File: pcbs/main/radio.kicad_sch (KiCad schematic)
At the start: 3 parts

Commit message: Re-routing
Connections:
- net +3V3 renamed +3.3V
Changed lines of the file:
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@@
 			)
 		)
-		(property "Value" "+3V3"
+		(property "Value" "+3.3V"
 			(at 35.5599 60.96 0)
 			(effects

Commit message: Fix pcb
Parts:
- C13: footprint PCM_Capacitor_THT_AKL:C_Disc_D5.0mm_W2.5mm_P2.50mm -> Capacitor_THT:C_Disc_D5.0mm_W2.5mm_P2.50mm
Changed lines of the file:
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@@
 		)
 		(instances
-			(project ""
+			(project "main"
 				(path "/8ab8953a-1156-4e8b-85bc-154005b38a27/95ef0ac5-d3bd-43eb-894b-cca92402ec9c"
 					(reference "PCB2")
@@
 		)
 		(instances
-			(project ""
+			(project "main"
 				(path "/8ab8953a-1156-4e8b-85bc-154005b38a27/95ef0ac5-d3bd-43eb-894b-cca92402ec9c"
 					(reference "PCB1")
@@
 		)
 		(instances
-			(project ""
+			(project "main"
 				(path "/8ab8953a-1156-4e8b-85bc-154005b38a27/95ef0ac5-d3bd-43eb-894b-cca92402ec9c"
 					(reference "#PWR039")
@@
 		)
 		(instances
-			(project ""
+			(project "main"
 				(path "/8ab8953a-1156-4e8b-85bc-154005b38a27/95ef0ac5-d3bd-43eb-894b-cca92402ec9c"
 					(reference "#PWR040")
@@
 			)
 		)
-		(property "Footprint" "PCM_Capacitor_THT_AKL:C_Disc_D5.0mm_W2.5mm_P2.50mm"
+		(property "Footprint" "Capacitor_THT:C_Disc_D5.0mm_W2.5mm_P2.50mm"
 			(at 48.26 67.6148 0)
 			(effects
@@
 		)
 		(instances
-			(project ""
+			(project "main"
 				(path "/8ab8953a-1156-4e8b-85bc-154005b38a27/95ef0ac5-d3bd-43eb-894b-cca92402ec9c"
 					(reference "C13")

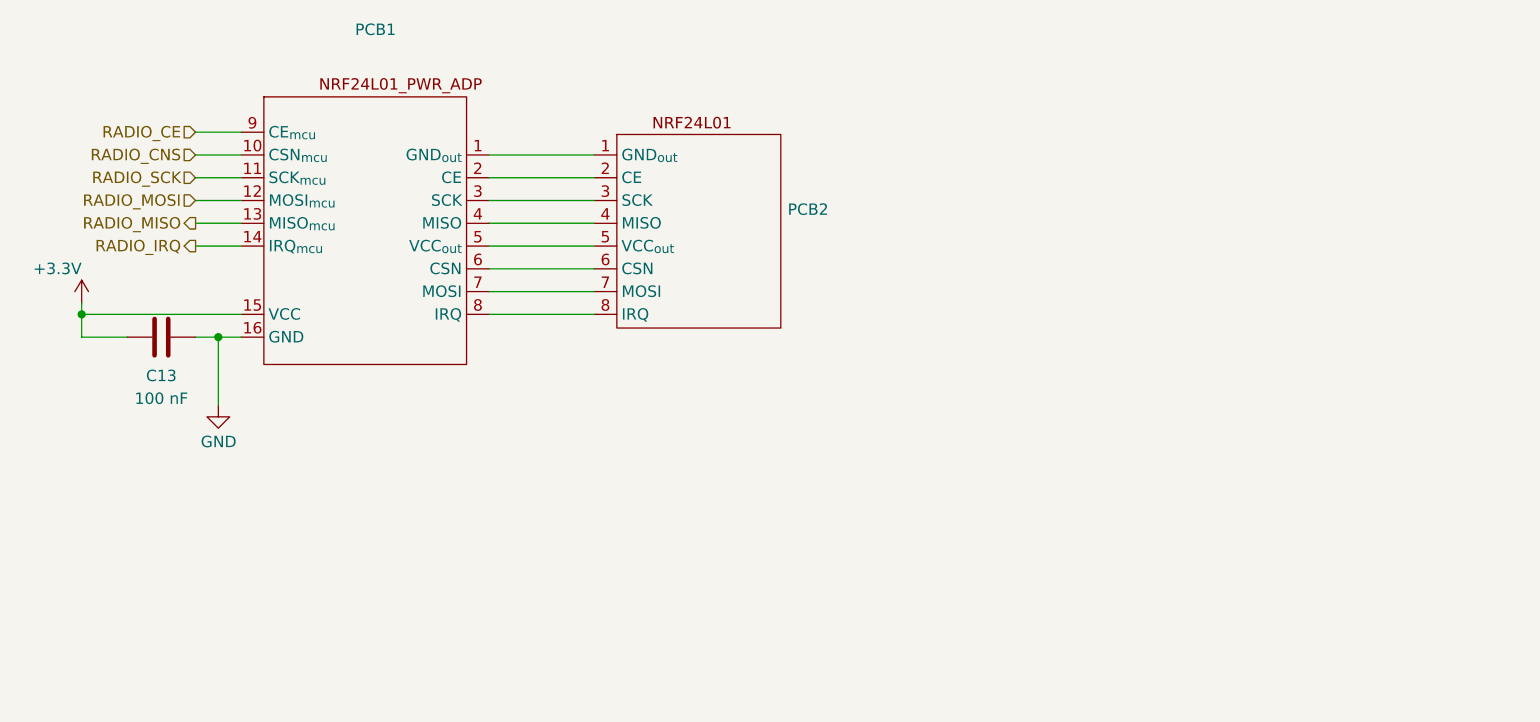
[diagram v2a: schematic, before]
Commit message: adding ldo regulador to radio
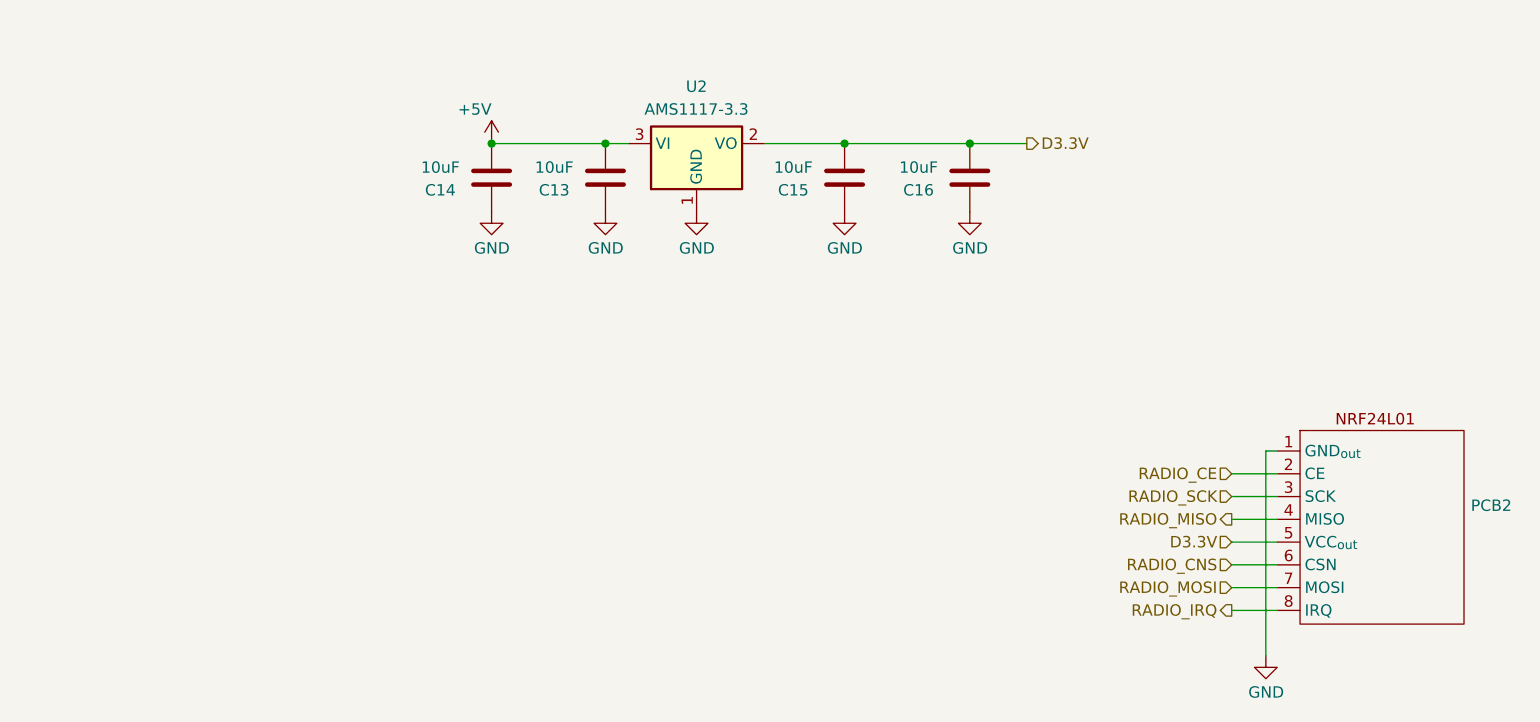
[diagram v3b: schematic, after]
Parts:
- removed PCB1: ~, Oxebots:NRF24L01_PWR_ADP, symbol oxebots:NRF24L01_PWR_ADP
- added C14, C15, C16: 10uF, Capacitor_SMD:C_1206_3216Metric, symbol Device:C
- added U2: AMS1117-3.3, Package_TO_SOT_SMD:SOT-223-3_TabPin2, symbol Regulator_Linear:AMS1117-3.3
- C13: value 100 nF -> 10uF; footprint Capacitor_THT:C_Disc_D5.0mm_W2.5mm_P2.50mm -> Capacitor_SMD:C_1206_3216Metric
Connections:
- net GND: now also PCB2.1 (GND_{out}), C14.2, C15.2, C16.2, U2.1 (GND)
- net RADIO_CE: now also PCB2.2 (CE)
- net RADIO_CNS: now also PCB2.6 (CSN)
- net RADIO_IRQ: now also PCB2.8 (IRQ)
- net RADIO_MISO: now also PCB2.4 (MISO)
- net RADIO_MOSI: now also PCB2.7 (MOSI)
- net RADIO_SCK: now also PCB2.3 (SCK)
- net D3.3V: now reaches PCB2.5 (VCC_{out})
- net D3.3V: now also C15.1, C16.1, U2.2 (VO)
- net +3.3V renamed +5V
- net +5V: now also C14.1, U2.3 (VI)
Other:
- moved on the sheet: C13, PCB2
